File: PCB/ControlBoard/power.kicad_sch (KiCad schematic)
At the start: 13 parts, among them U1 TPS259630, U4 AMS1117-3.3

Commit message: First pass of PCB rework.
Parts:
- C10, C4, C5, C9: footprint Capacitor_SMD:C_0805_2012Metric -> Capacitor_SMD:C_0603_1608Metric
- R1, R2, R4, R5, R6: footprint Resistor_SMD:R_0805_2012Metric -> Resistor_SMD:R_0603_1608Metric
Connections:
- net +BATT renamed VBUS

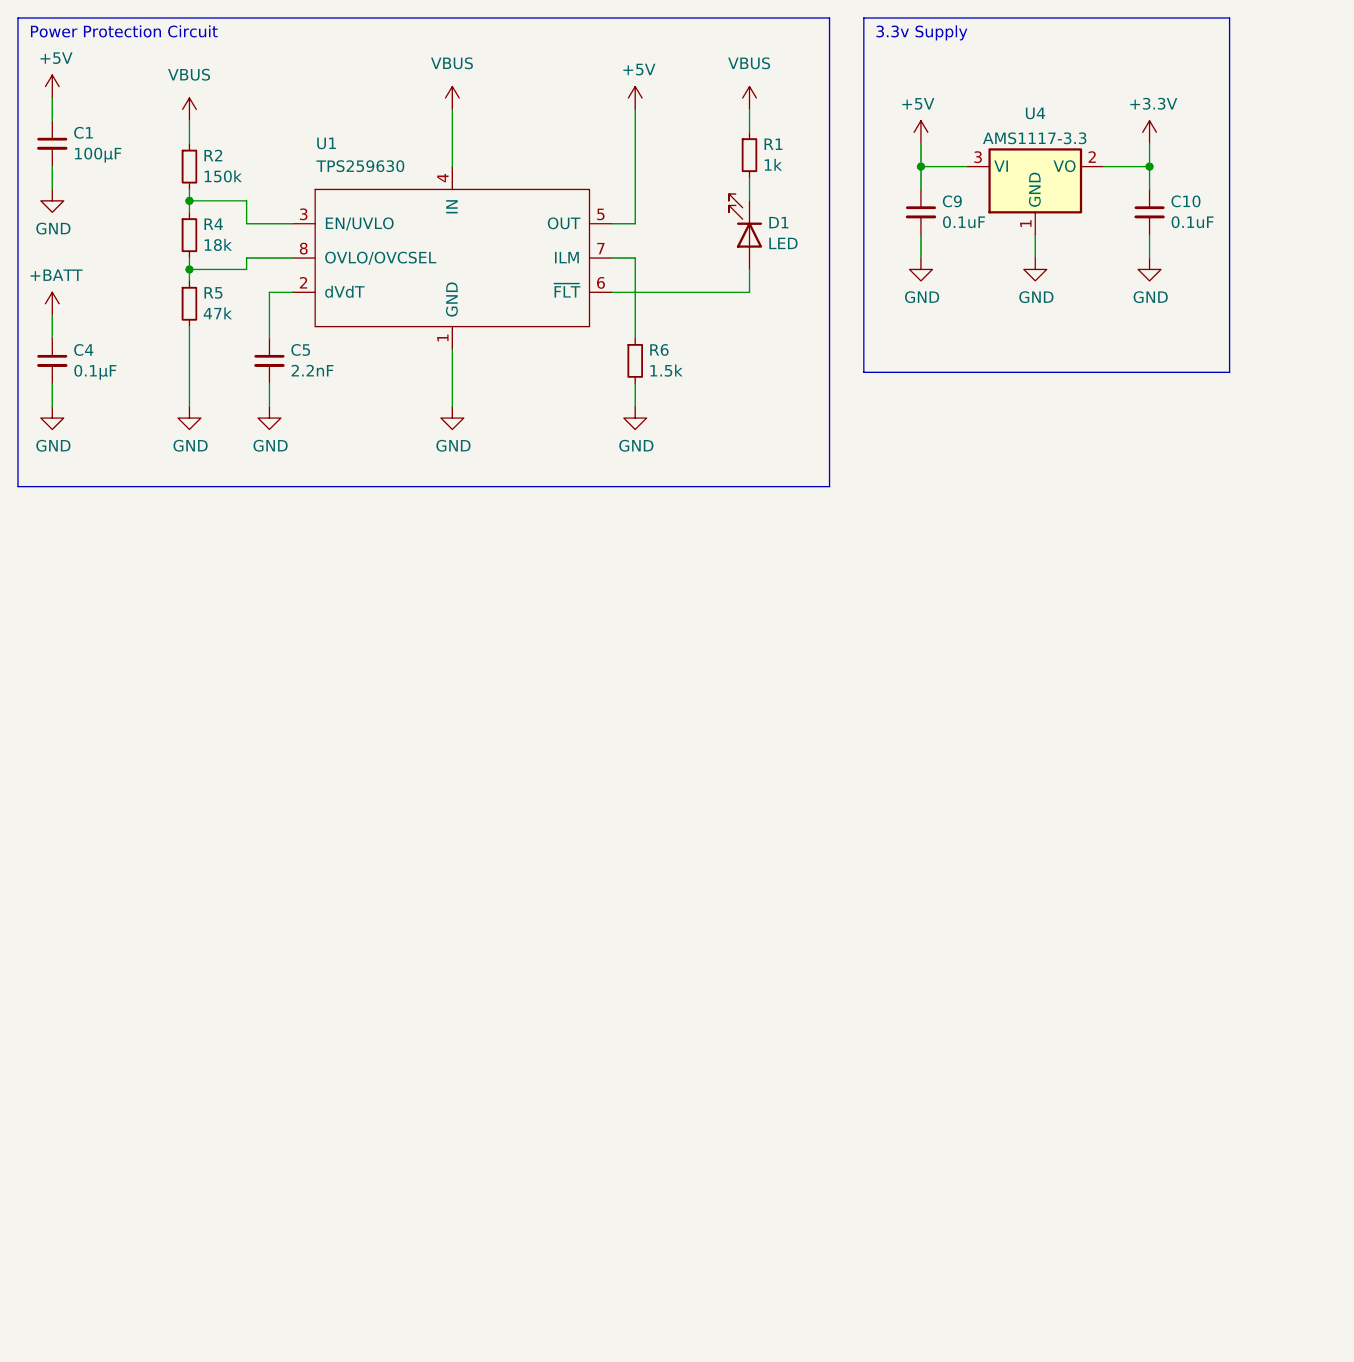
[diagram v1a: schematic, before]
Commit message: ControlBoard B02, with buck regulator fix.
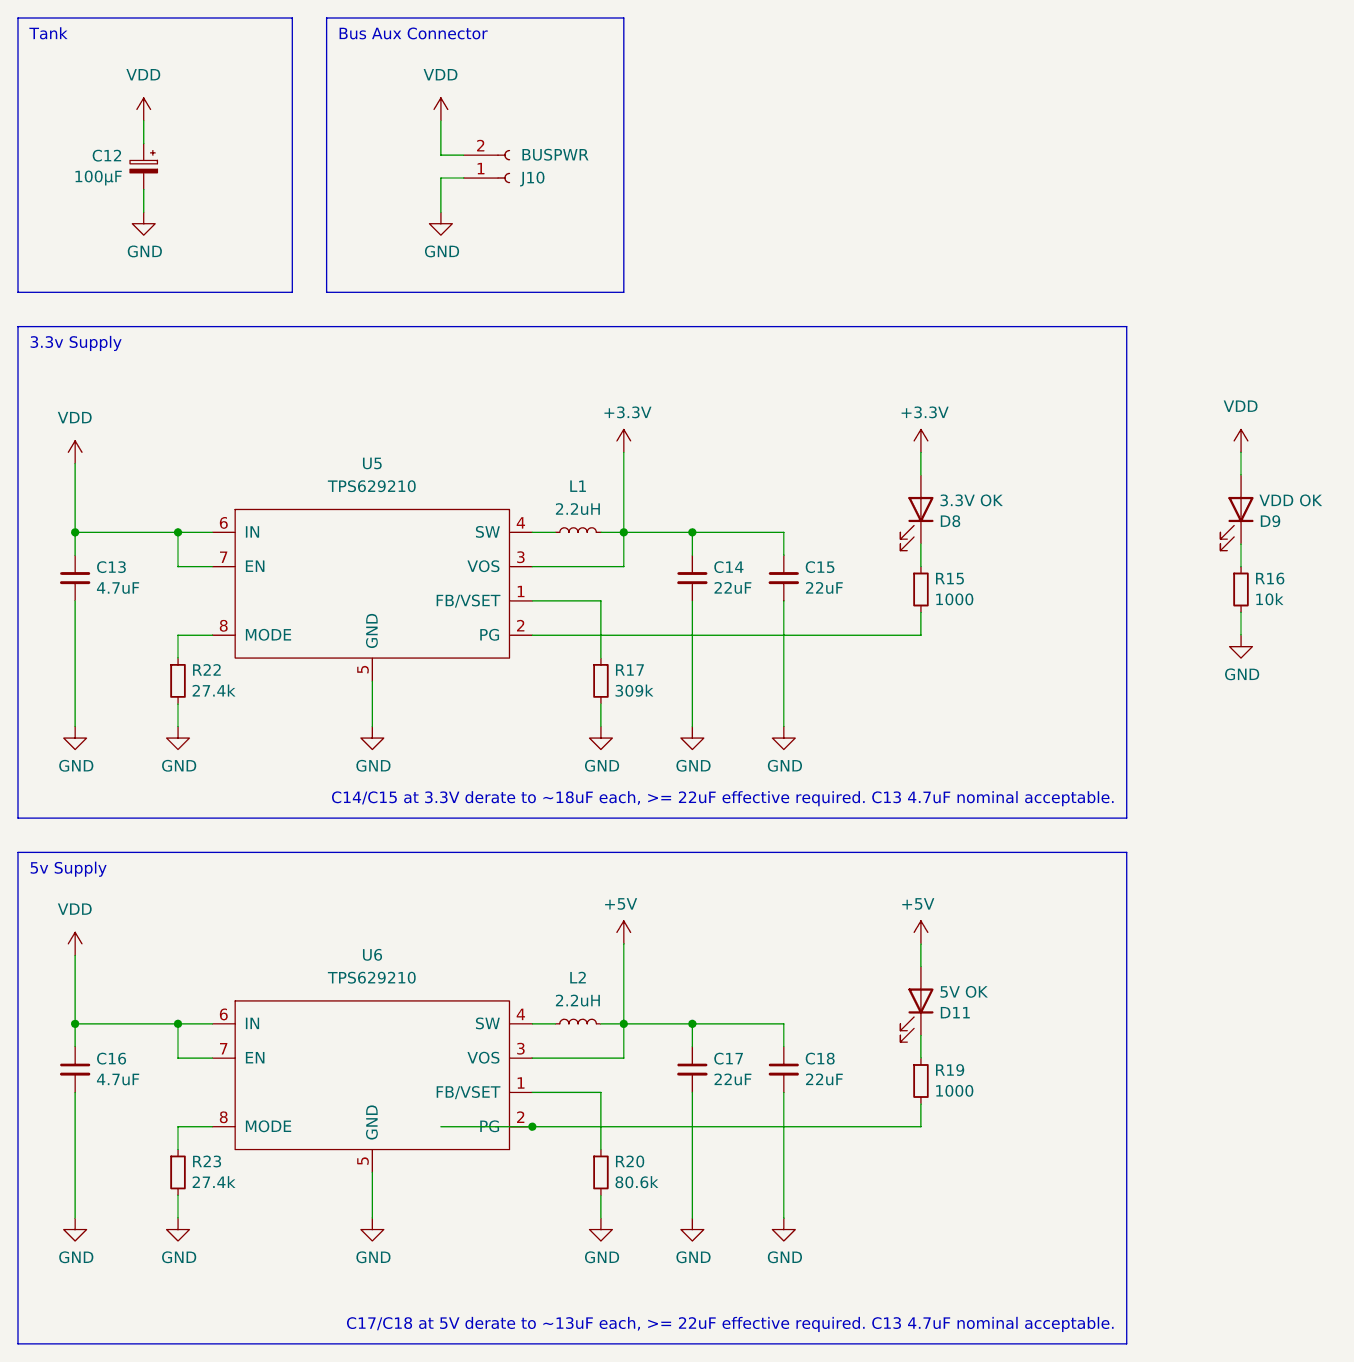
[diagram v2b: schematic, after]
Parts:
- removed C10, C9: 0.1uF, Capacitor_SMD:C_0603_1608Metric, symbol Device:C_Small
- removed C4: 0.1μF, Capacitor_SMD:C_0603_1608Metric, symbol Device:C_Small
- removed C5: 2.2nF, Capacitor_SMD:C_0603_1608Metric, symbol Device:C_Small
- removed D1: LED, LED_SMD:LED_0805_2012Metric, symbol Device:LED
- removed R1: 1k, Resistor_SMD:R_0603_1608Metric, symbol Device:R_Small
- removed R2: 150k, Resistor_SMD:R_0603_1608Metric, symbol Device:R_Small
- removed R4: 18k, Resistor_SMD:R_0603_1608Metric, symbol Device:R_Small
- removed R5: 47k, Resistor_SMD:R_0603_1608Metric, symbol Device:R_Small
- removed R6: 1.5k, Resistor_SMD:R_0603_1608Metric, symbol Device:R_Small
- removed U1: TPS259630, Package_SO:SOIC-8-1EP_3.9x4.9mm_P1.27mm_EP2.29x3mm, symbol KTANE:TPS25962X
- removed U4: AMS1117-3.3, Package_TO_SOT_SMD:SOT-223-3_TabPin2, symbol Regulator_Linear:AMS1117-3.3
- added C13, C16: 4.7uF, Capacitor_SMD:C_1206_3216Metric, symbol Device:C_Small
- added C14, C15, C17, C18: 22uF, Capacitor_SMD:C_1206_3216Metric, symbol Device:C_Small
- added D11: 5V OK, LED_SMD:LED_0603_1608Metric, symbol Device:LED
- added D8: 3.3V OK, LED_SMD:LED_0603_1608Metric, symbol Device:LED
- added D9: VDD OK, LED_SMD:LED_0603_1608Metric, symbol Device:LED
- added J10: BUSPWR, Connector_AMASS:AMASS_XT30PW-F_1x02_P2.50mm_Horizontal, symbol Connector:Conn_01x02_Socket
- added L1, L2: 2.2uH, Inductor_SMD:L_1008_2520Metric, symbol Device:L_Small
- added R15, R19: 1000, Resistor_SMD:R_0603_1608Metric, symbol Device:R_Small
- added R16: 10k, Resistor_SMD:R_0603_1608Metric, symbol Device:R_Small
- added R17: 309k, Resistor_SMD:R_0603_1608Metric, symbol Device:R_Small
- added R20: 80.6k, Resistor_SMD:R_0603_1608Metric, symbol Device:R_Small
- added R22, R23: 27.4k, Resistor_SMD:R_0603_1608Metric, symbol Device:R_Small
- added U5, U6: TPS629210, Package_TO_SOT_SMD:SOT-583-8, symbol KTANE:TPS6292XX
- C12: renamed from C1; footprint Capacitor_Tantalum_SMD:CP_EIA-7343-31_Kemet-D -> Capacitor_SMD:C_Elec_6.3x7.7; symbol Device:C_Small -> Device:C_Polarized_Small; DIGIKEY (none) -> 399-A768EB107M1ELAE036CT-ND
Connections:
- net +3.3V: now also C14.1, C15.1, D8.2 (A), L1.2, U5.3 (VOS)
- net +5V: now also C17.1, C18.1, D11.2 (A), L2.2, U6.3 (VOS); no longer C12.1
- net GND: now also C13.2, C14.2, C15.2, C16.2, C17.2, C18.2, J10.1 (Pin_1), R16.2, R17.2, R20.2, R22.2, R23.2, U5.5 (GND), U6.5 (GND)
- new net: R20.1, U6.1 (FB/VSET)
- new net: R19.2, U6.2 (PG)
- new net: L2.1, U6.4 (SW)
- new net: R23.1, U6.8 (MODE)
- new net: D11.1 (K), R19.1
- new net: D8.1 (K), R15.1
- new net: R15.2, U5.2 (PG)
- new net: D9.1 (K), R16.1
- new net: R22.1, U5.8 (MODE)
- new net: L1.1, U5.4 (SW)
- new net: R17.1, U5.1 (FB/VSET)
- new net VDD: C12.1, C13.1, C16.1, D9.2 (A), J10.2 (Pin_2), U5.6 (IN), U5.7 (EN), U6.6 (IN), U6.7 (EN)
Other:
- note added: "5v Supply"
- note added: "Bus Aux Connector"
- note added: "C14/C15 at 3.3V derate to ~18uF each, >= 22uF effective required. C13 4.7uF nominal acceptable."
- note added: "C17/C18 at 5V derate to ~13uF each, >= 22uF effective required. C13 4.7uF nominal acceptable."
- note added: "Tank"
- note removed: "Power Protection Circuit"

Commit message: Fix up power LEDs on regulators.
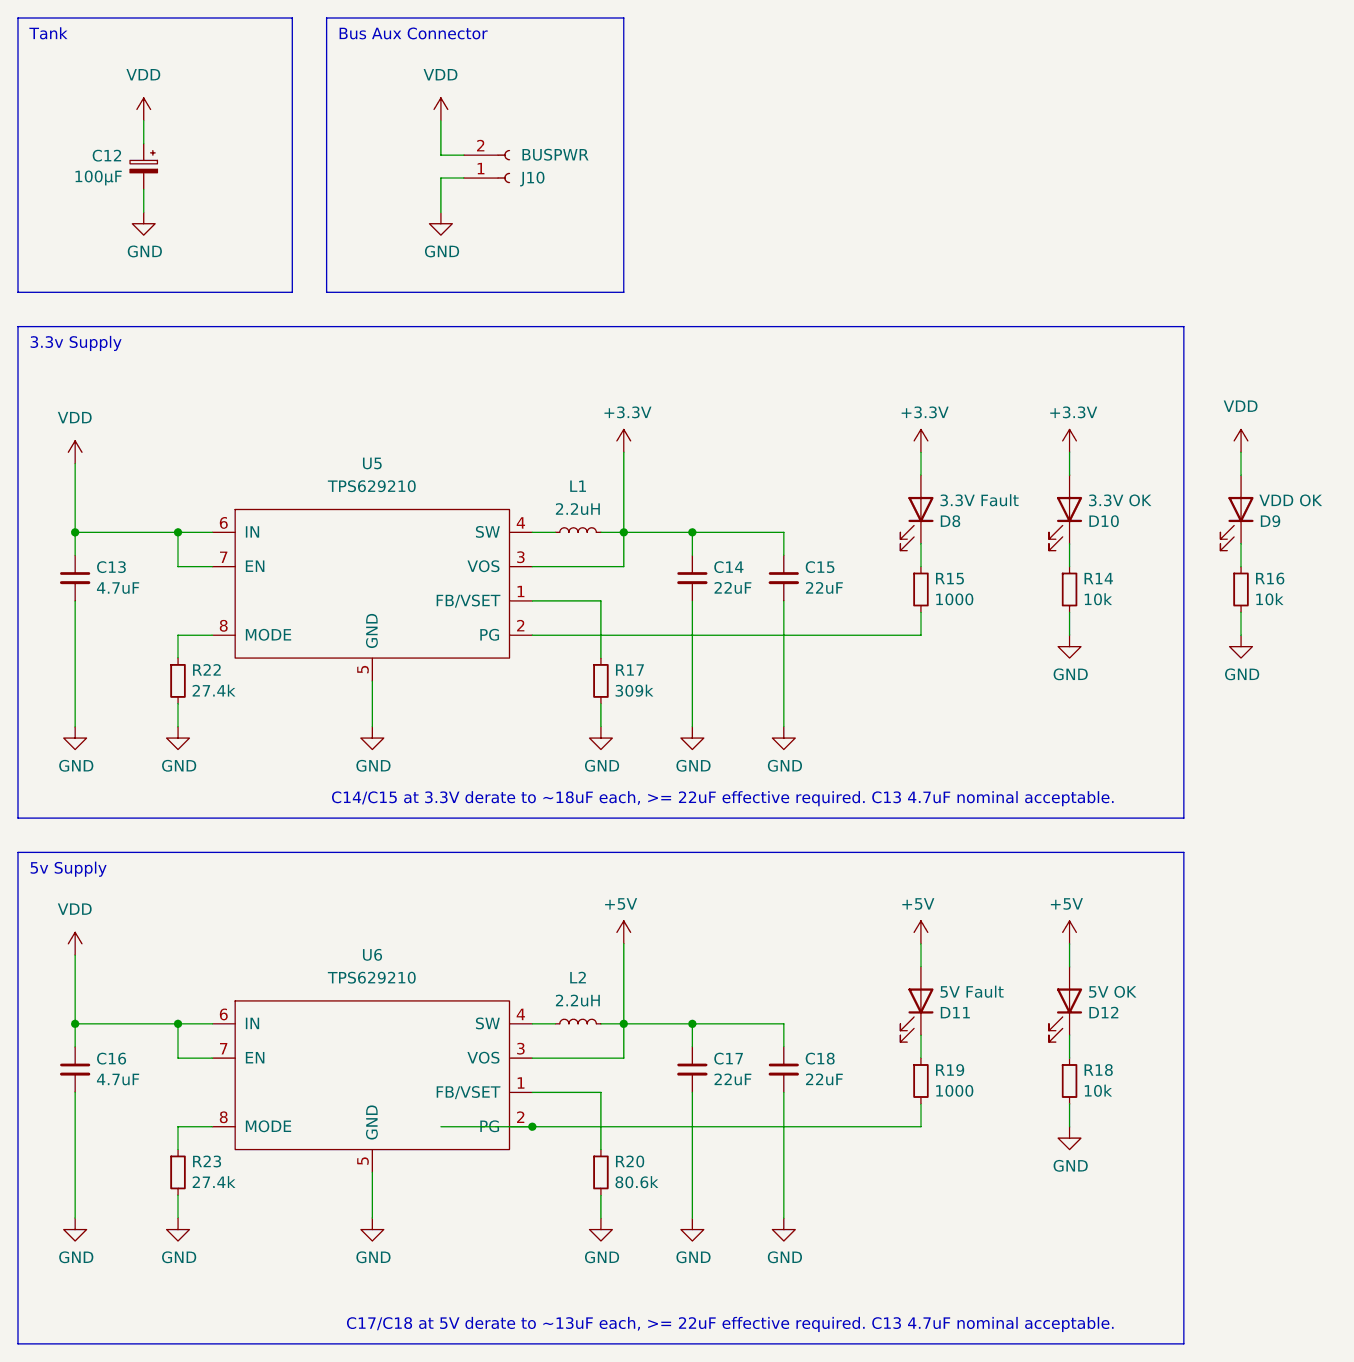
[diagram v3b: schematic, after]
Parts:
- added D10: 3.3V OK, LED_SMD:LED_0603_1608Metric, symbol Device:LED
- added D12: 5V OK, LED_SMD:LED_0603_1608Metric, symbol Device:LED
- added R14, R18: 10k, Resistor_SMD:R_0603_1608Metric, symbol Device:R_Small
- D11: value 5V OK -> 5V Fault; DIGIKEY 3147-B19Y1UYG-20C000313U1930CT-ND -> 3147-B19Y1USD-20C000113U1930CT-ND
- D8: value 3.3V OK -> 3.3V Fault; DIGIKEY 3147-B19Y1UYG-20C000313U1930CT-ND -> 3147-B19Y1USD-20C000113U1930CT-ND
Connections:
- net +3.3V: now also D10.2 (A)
- net +5V: now also D12.2 (A)
- net GND: now also R14.2, R18.2
- new net: D10.1 (K), R14.1
- new net: D12.1 (K), R18.1

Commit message: Correct Digikey part numbers.
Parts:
- J10: DIGIKEY STOCK -> STOCK/AMASS
- R14, R18: value 10k -> 1000; DIGIKEY P10.0KHCT-ND -> P1.00KHCT-ND
- R16: DIGIKEY P10.0KHCT-ND -> P10.0KHCT-ND
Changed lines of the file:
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@@
 	)
 	(junction
-		(at 72.39 138.43)
-		(diameter 0)
-		(color 0 0 0 0)
-	)
-	(junction
 		(at 82.55 127)
 		(diameter 0)
@@
 	(wire
 		(pts
-			(xy 62.23 138.43) (xy 72.39 138.43)
-		)
-		(stroke
-			(width 0)
-			(type default)
-		)
-	)
-	(wire
-		(pts
 			(xy 29.21 36.83) (xy 29.21 34.29)
 		)
@@
 			)
 		)
-		(property "DIGIKEY" "STOCK"
+		(property "DIGIKEY" "STOCK/AMASS"
 			(at 69.85 33.02 0)
 			(effects
@@
 			)
 		)
-		(property "Value" "10k"
+		(property "Value" "1000"
 			(at 133.5786 79.883 0)
 			(effects
@@
 			)
 		)
-		(property "DIGIKEY" "P10.0KHCT-ND "
+		(property "DIGIKEY" "P1.00KHCT-ND"
 			(at 132.08 78.74 0)
 			(effects
@@
 			)
 		)
-		(property "Value" "10k"
+		(property "Value" "1000"
 			(at 133.5786 134.493 0)
 			(effects
@@
 			)
 		)
-		(property "DIGIKEY" "P10.0KHCT-ND "
+		(property "DIGIKEY" "P1.00KHCT-ND"
 			(at 132.08 133.35 0)
 			(effects
@@
 			)
 		)
-		(property "DIGIKEY" "P10.0KHCT-ND "
+		(property "DIGIKEY" "P10.0KHCT-ND"
 			(at 151.13 78.74 0)
 			(effects
